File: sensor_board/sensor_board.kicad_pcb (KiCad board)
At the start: 2 copper layers, 88 x 42.4 mm, 45 parts, among them J1 zigbee connector, J2 SWD, J3 Grove-SCD41_Male, J4 Grove-SCD41_Male, J5 Lithium_battery_conn, Q1 SI2300DS, Q2 SI2301DS, U1 MCP6002-xMC, U2 MIC5365-3.3YC5, U3 STM32L051C8Tx

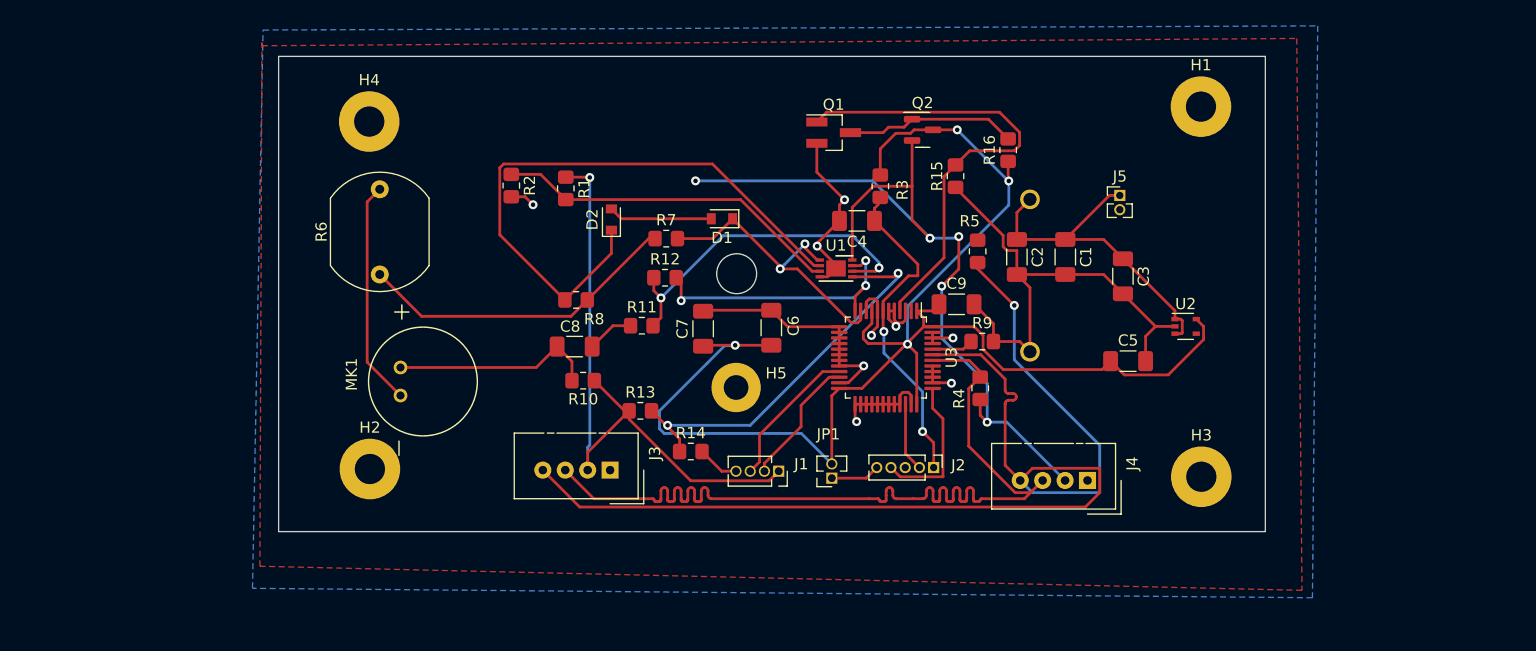
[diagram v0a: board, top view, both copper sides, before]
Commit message: replace 2 cells AA with single cell 18650 battery holder
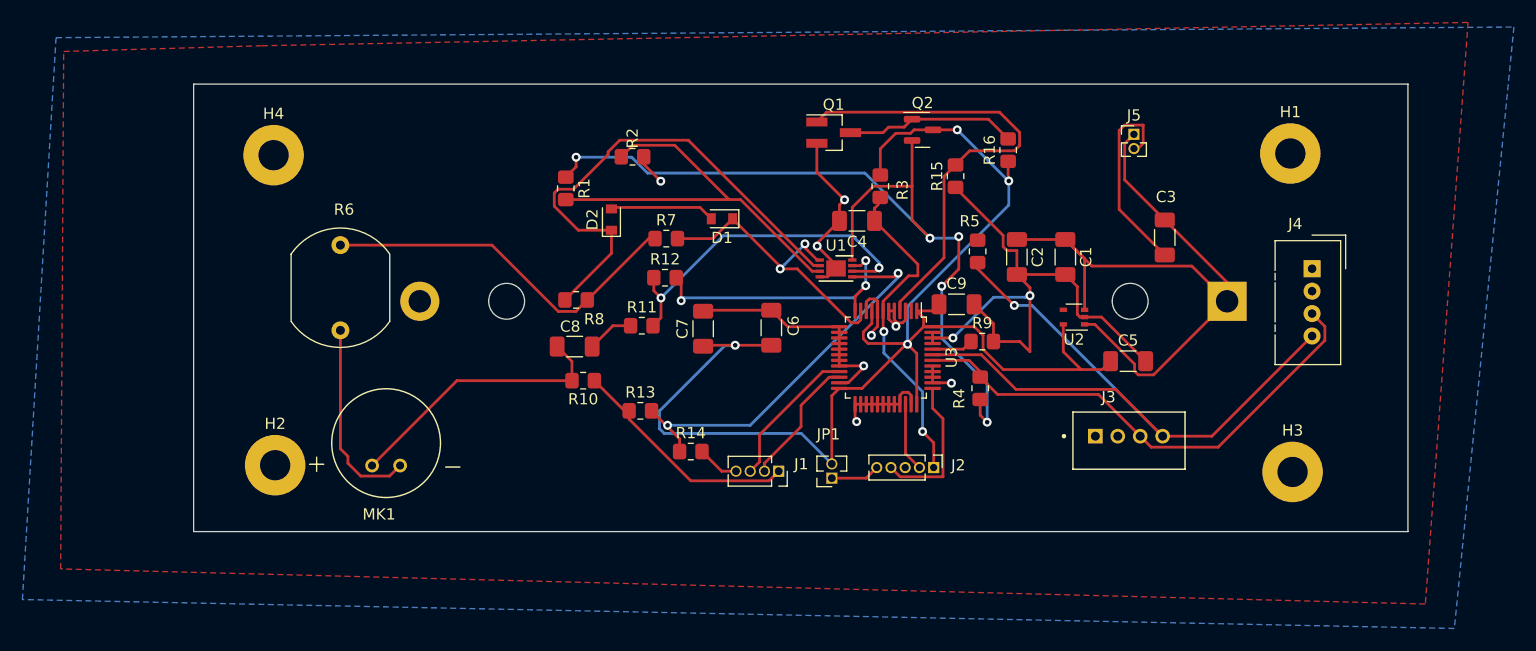
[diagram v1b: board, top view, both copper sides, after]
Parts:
- removed H5: MountingHole, MountingHole:MountingHole_2.2mm_M2_Pad
- BT1: value BC2AAPC -> Battery_Cell; footprint BC2AAPC:BAT_BC2AAPC -> Battery:BatteryHolder_MPD_BH-18650-PC2
- J1: value zigbee connector -> zigbee
- J3: value Grove-SCD41_Male -> 110990030; footprint Connector:NS-Tech_Grove_1x04_P2mm_Vertical -> 1x4 grove:SEEED_110990030
- J4: value Grove-SCD41_Male -> AM2320
- MK1: value AOM-6738P-R -> Mic
- R6: value LDR03 -> LDR03-Light
- moved J3 46.4 mm to (182.3, 90.7), turned to 0 degrees
- moved BT1 43.8 mm to (191.1, 78.7)
- moved J4 27.5 mm to (198.6, 75.7), turned to 0 degrees
- moved R2 11.1 mm to (138.0, 65.8), turned to 0 degrees
- moved U2 9.99 mm to (177.4, 80.1), turned to 180 degrees
- moved H4 9.04 mm to (106.0, 65.6)
- moved H1 9.00 mm to (196.7, 65.5)
- moved H2 8.46 mm to (106.2, 93.3)
- moved H3 8.15 mm to (196.9, 93.9)
- moved MK1 6.40 mm to (116.1, 91.3), turned to 180 degrees
- moved J5 5.59 mm to (182.8, 63.8)
- moved C3 5.09 mm to (185.5, 73.0)
- moved R6 4.38 mm to (112.0, 73.6), turned to -90 degrees
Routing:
- net SDA: track 112.2 -> 63.8 mm
- net SCL: track 81.6 -> 45.3 mm
- net V_bat: track 30.5 -> 64.7 mm
- net 3.3V_SENS: track 132.3 -> 101.8 mm, vias 6 -> 5
- net SDI: track 157.5 -> 178.6 mm, vias 9 -> 10
- net Net-(D2-Pad1): track 54.6 -> 45.5 mm
- net 3.3V: track 134.8 -> 127.3 mm
- net Net-(R1-Pad2): track 31.1 -> 37.3 mm
- net Net-(C8-Pad1): track 18.3 -> 24.5 mm
- net Net-(R6-Pad1): track 29.0 -> 33.2 mm
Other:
- board size 88 x 42.4 mm -> 108.3 x 39.9 mm

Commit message: modified:   sensor_board/sensor_board.kicad_pcb 	modified:   sensor_board/sensor_board.kicad_sch Fix SDI pins wiring error
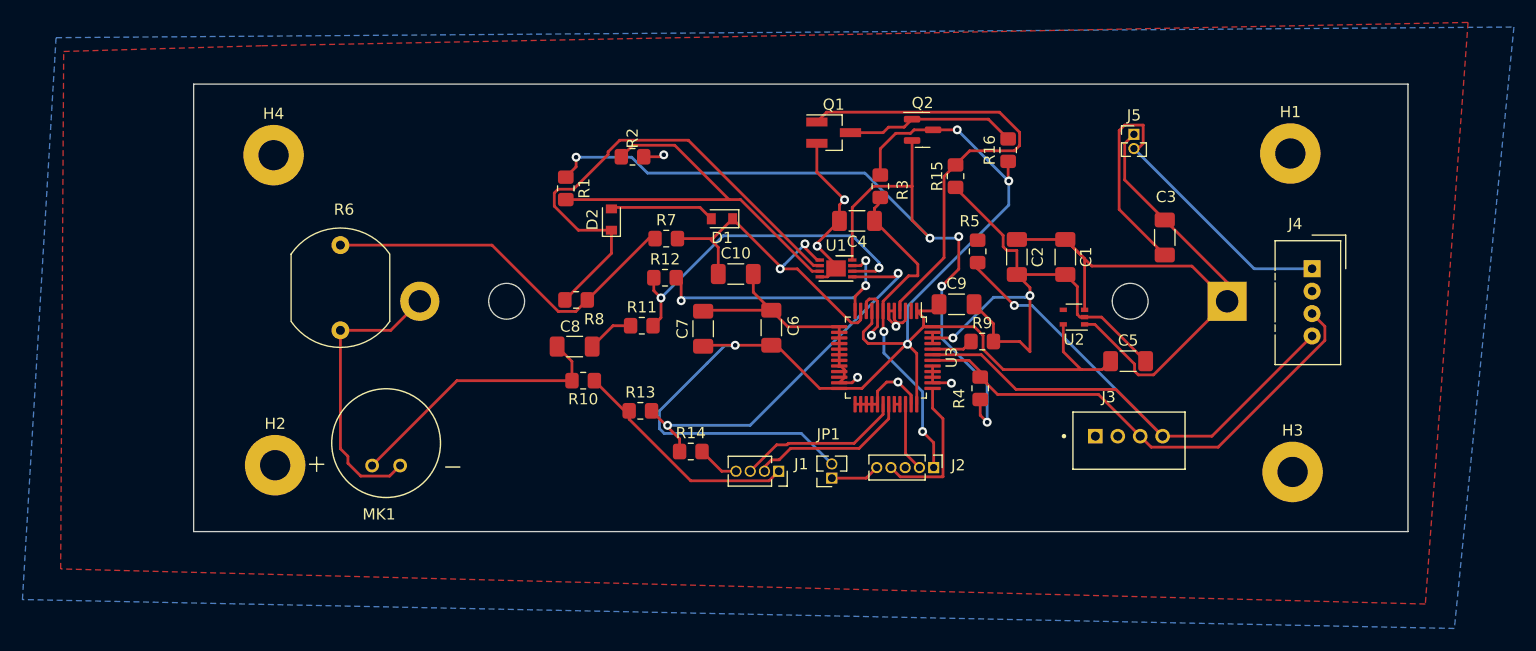
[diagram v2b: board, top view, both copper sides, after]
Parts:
- added C10: 0.1u, Capacitor_SMD:C_1206_3216Metric_Pad1.33x1.80mm_HandSolder, F.Cu at (147.2, 76.2)
- D1, D2: value D_Zener -> 1N4728
- J1: value zigbee -> zigbee connector
- MK1: value Mic -> AOM-6738P-R
- R6: value LDR03-Light -> LDR03
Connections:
- BT1 pad 2: SDI -> GND
- C1 pad 2: SDI -> GND
- C2 pad 2: SDI -> GND
- C3 pad 2: SDI -> GND
- C4 pad 2: SDI -> GND
- C5 pad 2: SDI -> GND
- C6 pad 2: SDI -> GND
- C7 pad 2: SDI -> GND
- C9 pad 2: SDI -> GND
- J1 pad 2: SDI -> SDO
- J1 pad 4: SDI -> GND
- J2 pad 3: SDI -> GND
- J3 pad 1: SDI -> GND
- J4 pad 1: SDI -> GND
- J5 pad 2: SDI -> GND
- MK1 pad N: SDI -> GND
- Q1 pad 2: SDI -> GND
- R14 pad 2: SDI -> GND
- R15 pad 1: SDI -> GND
- R2 pad 2: SDI -> GND
- R6 pad 2: SDI -> GND
- R9 pad 2: SDI -> GND
- U1 pad 4: SDI -> GND
- U1 pad 9: SDI -> GND
- U2 pad 2: SDI -> GND
- U3 pad 10: SDI -> GND
- U3 pad 13: SDI -> GND
- U3 pad 14: SDI -> GND
- U3 pad 15: SDI -> GND
- U3 pad 16: SDI -> GND
- U3 pad 17: SDI -> GND
- U3 pad 18: SDI -> GND
- U3 pad 19: SDI -> GND
- U3 pad 20: SDI -> GND
- U3 pad 21: SDI -> GND
- U3 pad 22: SDI -> GND
- U3 pad 23: SDI -> GND
- U3 pad 25: SDI -> GND
- U3 pad 26: SDI -> GND
- U3 pad 27: SDI -> GND
- U3 pad 28: SDI -> GND
- U3 pad 29: SDI -> GND
- U3 pad 3: SDI -> GND
- U3 pad 31: SDI -> SDO
- U3 pad 32: SDI -> Net-(U3-Pad32)
- U3 pad 33: SDI -> Net-(U3-Pad32)
- U3 pad 35: SDI -> GND
- U3 pad 38: SDI -> GND
- U3 pad 39: SDI -> GND
- U3 pad 40: SDI -> GND
- U3 pad 41: SDI -> GND
- U3 pad 45: SDI -> GND
- U3 pad 46: SDI -> GND
- U3 pad 47: SDI -> GND
- U3 pad 5: SDI -> GND
- U3 pad 6: SDI -> GND
- U3 pad 8: SDI -> GND
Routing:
- net GND: track 0.00 -> 183.5 mm, vias 0 -> 10
- net SDI: track 178.6 -> 14.8 mm, vias 10 -> 0
- net SDO: track 0.00 -> 14.5 mm
- net Vpr: track 27.3 -> 30.6 mm
- net 3.3V: track 127.3 -> 128.0 mm
- net Net-(U3-Pad32): track 0.00 -> 0.50 mm
- added copper zone on B.Cu, net GND
- removed copper zone on B.Cu, net SDI

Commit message: 1. modify schematic, replace mosfet which control sensors power with LDO IC 2. add accelerator sensor to measure wind speed 3. ..
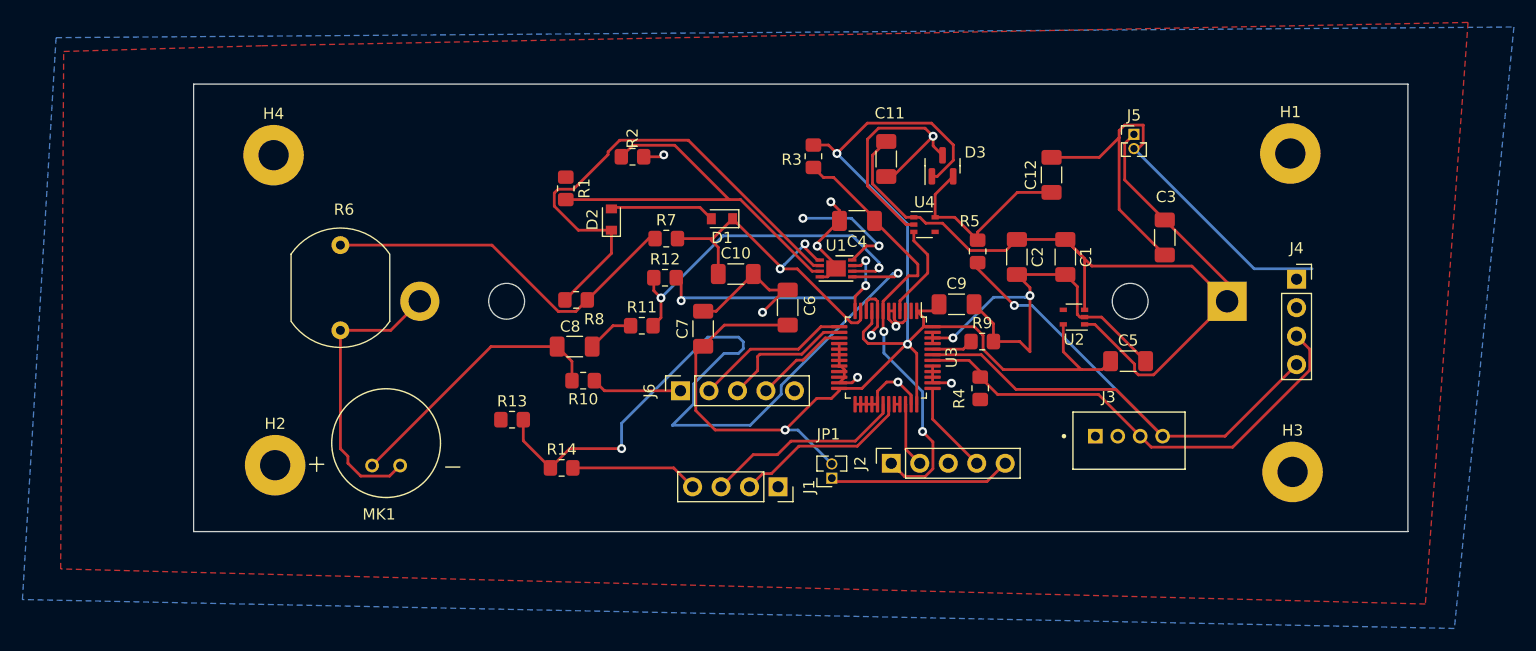
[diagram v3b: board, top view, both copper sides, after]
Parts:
- removed Q1: SI2300DS, Package_TO_SOT_SMD:SOT-23_Handsoldering
- removed Q2: SI2301DS, Package_TO_SOT_SMD:SOT-23
- removed R15: 10k, Resistor_SMD:R_0805_2012Metric_Pad1.20x1.40mm_HandSolder
- removed R16: 100k, Resistor_SMD:R_0805_2012Metric_Pad1.20x1.40mm_HandSolder
- added C11: 1u, Capacitor_SMD:C_1206_3216Metric_Pad1.33x1.80mm_HandSolder, F.Cu at (160.7, 66.0)
- added C12: 1u, Capacitor_SMD:C_1206_3216Metric_Pad1.33x1.80mm_HandSolder, F.Cu at (175.4, 67.4)
- added D3: D_Zener_Dual_CommonAnode_KKA, Package_TO_SOT_SMD:SOT-23, F.Cu at (165.7, 66.6)
- added J6: SWD, Connector_PinSocket_2.54mm:PinSocket_1x05_P2.54mm_Vertical, F.Cu at (142.3, 86.6)
- added U4: MIC5365-3.3YC5, Package_TO_SOT_SMD:SOT-353_SC-70-5, F.Cu at (164.1, 71.8)
- J1: footprint Connector_PinSocket_1.27mm:PinSocket_1x04_P1.27mm_Vertical -> Connector_PinSocket_2.54mm:PinSocket_1x04_P2.54mm_Vertical
- J2: footprint Connector_PinHeader_1.27mm:PinHeader_1x05_P1.27mm_Vertical -> Connector_PinSocket_2.54mm:PinSocket_1x05_P2.54mm_Vertical
- J4: footprint Connector:NS-Tech_Grove_1x04_P2mm_Vertical -> Connector_PinSocket_2.54mm:PinSocket_1x04_P2.54mm_Vertical
- moved R14 11.6 mm to (131.7, 93.5)
- moved R13 11.5 mm to (127.3, 89.2)
- moved R3 6.54 mm to (154.2, 65.7)
- moved J2 3.80 mm to (161.1, 93.1), turned to 90 degrees
- moved C6 2.32 mm to (151.9, 79.2)
- moved J4 1.67 mm to (197.3, 76.7)
- moved J1 1.39 mm to (151.0, 95.2)
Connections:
- U3 pad 13: GND -> Gx
- U3 pad 14: GND -> Gy
- U3 pad 15: GND -> Gz
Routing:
- net 3.3V_SENS: track 101.8 -> 36.5 mm, vias 5 -> 2
- net Net-(R13-Pad2): track 35.3 -> 70.1 mm
- net SENSORS_EN: track 41.9 -> 8.59 mm
- net V_bat: track 64.7 -> 84.7 mm
- net GND: track 183.5 -> 199.6 mm, vias 10 -> 12
- net Net-(Q1-Pad3): track 15.3 -> 0.00 mm
- net Gx: track 0.00 -> 14.0 mm
- net Gy: track 0.00 -> 12.0 mm
- net Net-(J2-Pad5): track 4.40 -> 16.3 mm
- net NRST: track 28.9 -> 39.4 mm
- net Gz: track 0.00 -> 8.49 mm
- net SWCLK: track 13.2 -> 8.31 mm
- net 3.3V: track 128.0 -> 123.4 mm, vias 4 -> 3
- net SDI: track 14.8 -> 18.0 mm
- net SDA: track 63.8 -> 61.3 mm
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
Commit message: 1. use sensorion scd42 for lower power 2. add usb micro B for testing or using with backup battery later 3. add signal RC filter
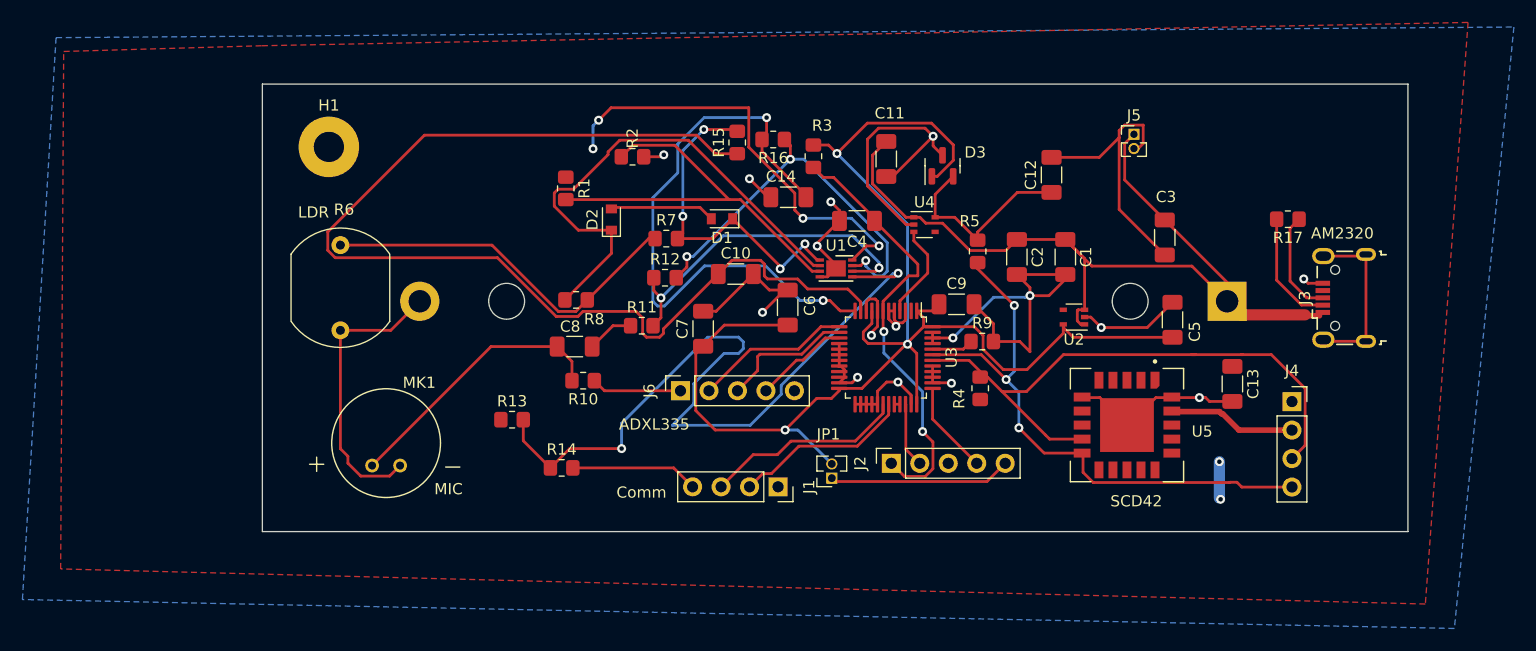
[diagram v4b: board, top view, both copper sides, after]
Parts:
- removed H2, H3, H4: MountingHole, MountingHole:MountingHole_2.7mm_M2.5_Pad
- added C13: 1u, Capacitor_SMD:C_1206_3216Metric_Pad1.33x1.80mm_HandSolder, F.Cu at (191.5, 86.0)
- added C14: 1n, Capacitor_SMD:C_1206_3216Metric_Pad1.33x1.80mm_HandSolder, F.Cu at (151.9, 69.4)
- added R15: 20k, Resistor_SMD:R_0805_2012Metric_Pad1.20x1.40mm_HandSolder, F.Cu at (147.4, 64.5)
- added R16: 4.7k, Resistor_SMD:R_0805_2012Metric_Pad1.20x1.40mm_HandSolder, F.Cu at (150.6, 64.2)
- added R17: 200, Resistor_SMD:R_0805_2012Metric_Pad1.20x1.40mm_HandSolder, F.Cu at (196.5, 71.3)
- added U5: SDC42, SCD41-D-R2:XDCR_SCD41-D-R2, F.Cu at (182.1, 89.7)
- C10: value 0.1u -> 1u
- J3: value 110990030 -> USB_B_Micro; footprint 1x4 grove:SEEED_110990030 -> Connector_USB:USB_Micro-B_Wuerth_629105150521
- J6: value SWD -> ACC
- moved H1 85.8 mm to (111.0, 64.9)
- moved J3 22.8 mm to (201.5, 78.3), turned to 90 degrees
- moved J4 10.9 mm to (196.8, 87.6)
- moved C5 5.41 mm to (186.2, 80.3), turned to 90 degrees
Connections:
- D1 pad 1: Vpr -> Net-(D1-Pad1)
- J3 pad 1: GND -> V_bat
- J3 pad 2: 3.3V_SENS -> Net-(J3-Pad2)
- J3 pad 3: SCL -> Net-(J3-Pad3)
- J3 pad 4: SDA -> unconnected-(J3-Pad4)
- R12 pad 2: MIC -> Net-(R12-Pad2)
- R7 pad 2: Vpr -> Net-(D1-Pad1)
- U1 pad 1: Vpr -> Net-(D1-Pad1)
- U1 pad 7: MIC -> Net-(R12-Pad2)
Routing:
- net Vpr: track 30.6 -> 100.4 mm, vias 2 -> 0
- net 3.3V_SENS: track 36.5 -> 79.7 mm, vias 2 -> 6
- net Net-(R12-Pad2): track 0.00 -> 35.7 mm, vias 0 -> 3
- net Net-(D1-Pad1): track 0.00 -> 30.9 mm, vias 0 -> 4
- net MIC: track 25.5 -> 54.1 mm, vias 3 -> 2
- net unconnected-(J3-Pad6): track 0.00 -> 15.5 mm
- net Net-(J3-Pad2): track 0.00 -> 10.5 mm
- net SCL: track 43.5 -> 53.4 mm
- net SDA: track 61.3 -> 51.7 mm, vias 1 -> 3
- net Net-(J3-Pad3): track 0.00 -> 9.40 mm
- net V_bat: track 84.7 -> 78.6 mm
- net 3.3V: track 123.4 -> 126.5 mm
- net GND: track 199.6 -> 200.8 mm, vias 12 -> 16
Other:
- board size 108.3 x 39.9 mm -> 102.2 x 39.9 mm
- board text added: "ADXL335"
- board text added: "AM2320"
- board text added: "Comm"
- board text added: "LDR"
- board text added: "MIC"
- board text added: "SCD42"
